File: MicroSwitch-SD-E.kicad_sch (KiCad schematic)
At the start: 4 parts, among them J1 Conn_01x03_Pin, Q1 BSS84, U1 A3144

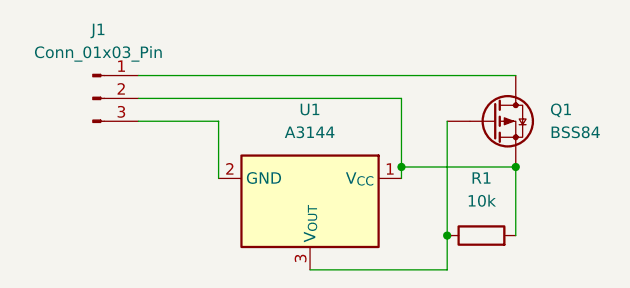
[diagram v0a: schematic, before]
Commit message: fix: change 10k to 11k for consistency
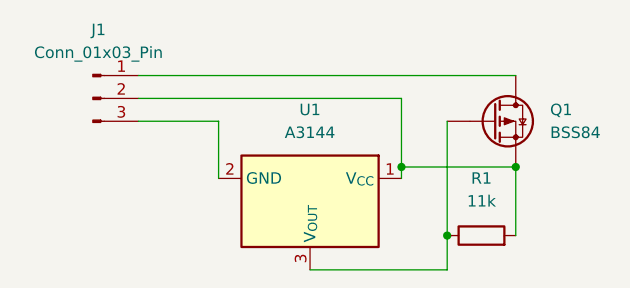
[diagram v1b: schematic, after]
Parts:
- R1: value 10k -> 11k
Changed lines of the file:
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@@
 			)
 		)
-		(property "Value" "10k"
+		(property "Value" "11k"
 			(at 129.54 102.87 90)
 			(show_name no)
